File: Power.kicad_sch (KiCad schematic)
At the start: 21 parts

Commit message: Reset switch added
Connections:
- net 5V: no longer CP7.1, CP8.1, CP9.1, LP3.2, RP5.1, UP1.2 (VBIAS)
- new net MOT_POW: CP7.1, CP8.1, CP9.1, LP3.2, RP5.1, UP1.2 (VBIAS)
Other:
- note removed: "We need Motor power to be above 5 V say 5.2 or 5.5"
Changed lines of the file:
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@@
     (effects (font (size 1.778 1.778)) (justify left bottom))
   )
-  (text "We need Motor power to\nbe above 5 V say 5.2 or 5.5 \n"
-    (at 64.77 177.8 0)
-    (effects (font (size 1.27 1.27)) (justify left bottom))
-  )
-  (label "5V" (at 150.495 128.27 180)
+  (label "5V3" (at 150.495 128.27 180)
     (effects (font (size 1.27 1.27)) (justify right bottom))
   )

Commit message: MCU interfaces pulled out to parent sheet
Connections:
- net MCU_POW renamed 3V3
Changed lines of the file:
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@@
   (junction (at 138.43 139.7) (diameter 0) (color 0 0 0 0)
+  )
+  (junction (at 179.07 96.52) (diameter 0) (color 0 0 0 0)
   )
   (no_connect (at 107.95 132.08))
@@
     (stroke (width 0) (type default) (color 0 0 0 0))
   )
+  (wire (pts (xy 179.07 101.6) (xy 179.07 96.52))
+    (stroke (width 0) (type default) (color 0 0 0 0))
+  )
   (wire (pts (xy 114.935 35.56) (xy 120.65 35.56))
     (stroke (width 0) (type default) (color 0 0 0 0))
@@
   )
   (wire (pts (xy 138.43 164.465) (xy 138.43 168.275))
+    (stroke (width 0) (type default) (color 0 0 0 0))
+  )
+  (wire (pts (xy 196.85 101.6) (xy 179.07 101.6))
     (stroke (width 0) (type default) (color 0 0 0 0))
   )
@@
     (effects (font (size 1.27 1.27)) (justify left))
   )
+  (hierarchical_label "3V3" (shape bidirectional) (at 196.85 101.6 0)
+    (effects (font (size 1.27 1.27)) (justify left))
+  )

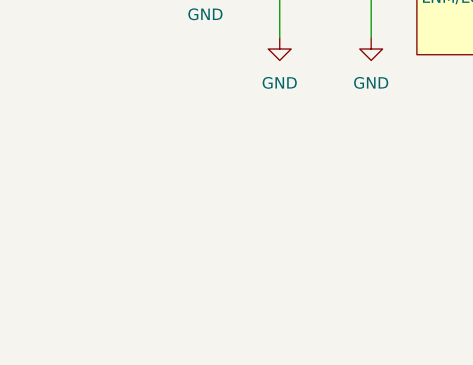
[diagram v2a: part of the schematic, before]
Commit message: MCU interfaces are done! Check the Changes and Complete ERC modifications
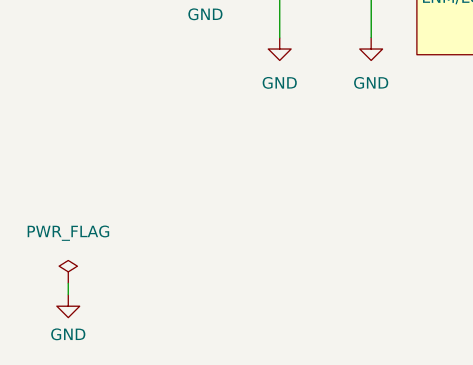
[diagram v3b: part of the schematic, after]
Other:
- company: (none) -> Parikshit Student Satellite Team
- title: (none) -> AOCS BOARD
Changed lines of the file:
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@@
 (kicad_sch (version 20211123) (generator eeschema)
   (paper "A4")
+  (title_block
+    (title "AOCS BOARD")
+    (company "Parikshit Student Satellite Team")
+  )
   (junction (at 63.5 33.02) (diameter 0) (color 0 0 0 0)
   )
@@
   )
   (wire (pts (xy 179.07 96.52) (xy 196.85 96.52))
+    (stroke (width 0) (type default) (color 0 0 0 0))
+  )
+  (wire (pts (xy 32.385 177.8) (xy 32.385 176.53))
     (stroke (width 0) (type default) (color 0 0 0 0))
   )
@@
     (pin "1")
   )
+  (symbol (lib_id "power:GND") (at 32.385 177.8 0) (unit 1)
+    (in_bom yes) (on_board yes) (fields_autoplaced)
+    (property "Reference" "#PWR0273" (id 0) (at 32.385 184.15 0)
+      (effects (font (size 1.27 1.27)) hide)
+    )
+    (property "Value" "GND" (id 1) (at 32.385 182.245 0))
+    (property "Footprint" "" (id 2) (at 32.385 177.8 0)
+      (effects (font (size 1.27 1.27)) hide)
+    )
+    (property "Datasheet" "" (id 3) (at 32.385 177.8 0)
+      (effects (font (size 1.27 1.27)) hide)
+    )
+    (pin "1")
+  )
   (symbol (lib_id "Device:C") (at 60.96 140.97 90) (unit 1)
     (in_bom yes) (on_board yes) (fields_autoplaced)
@@
     (pin "2")
   )
+  (symbol (lib_id "power:PWR_FLAG") (at 32.385 176.53 0) (unit 1)
+    (in_bom yes) (on_board yes) (fields_autoplaced)
+    (property "Reference" "#FLG0109" (id 0) (at 32.385 174.625 0)
+      (effects (font (size 1.27 1.27)) hide)
+    )
+    (property "Value" "PWR_FLAG" (id 1) (at 32.385 170.815 0))
+    (property "Footprint" "" (id 2) (at 32.385 176.53 0)
+      (effects (font (size 1.27 1.27)) hide)
+    )
+    (property "Datasheet" "~" (id 3) (at 32.385 176.53 0)
+      (effects (font (size 1.27 1.27)) hide)
+    )
+    (pin "1")
+  )
   (symbol (lib_id "power:GND") (at 170.18 45.085 0) (unit 1)

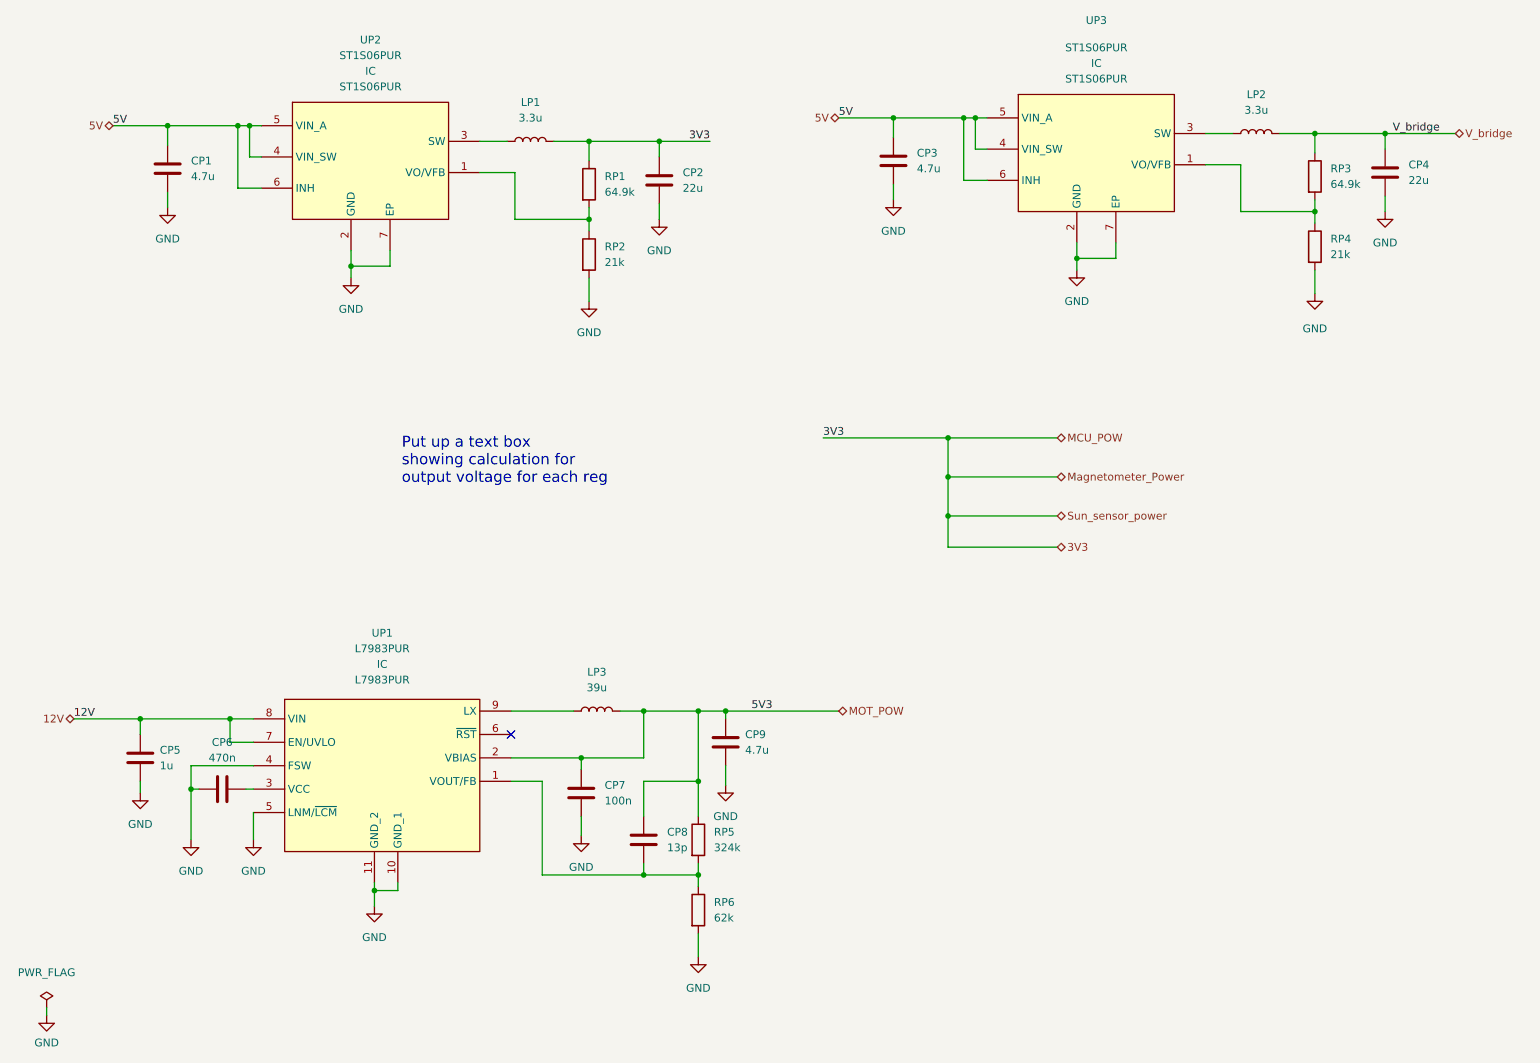
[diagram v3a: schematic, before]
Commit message: Max ERC errors corrected
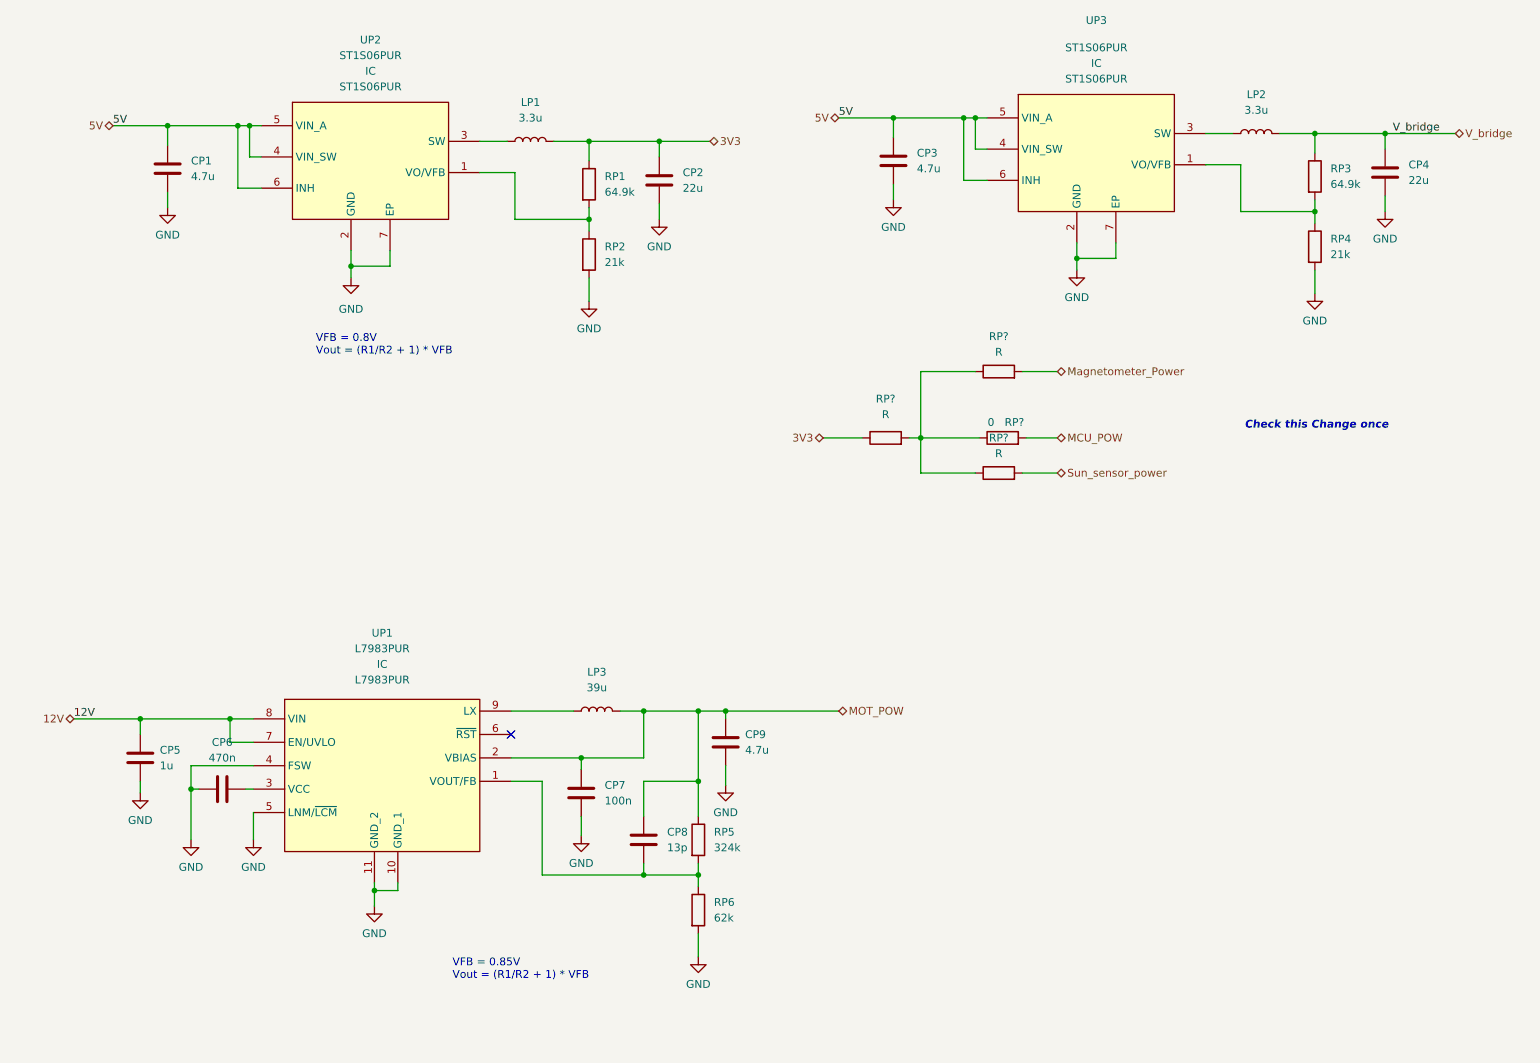
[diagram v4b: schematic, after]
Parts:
- added RP? (x3): R, symbol Device:R
- added RP?: 0, symbol Device:R
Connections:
- net 3V3: now also RP?.1
- new net: RP?.1, RP?.1, RP?.1, RP?.2
- new net MCU_POW: RP?.2
- new net Magnetometer_Power: RP?.2
- new net Sun_sensor_power: RP?.2
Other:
- note added: "Check this Change once"
- note added: "VFB = 0.85V Vout = (R1/R2 + 1) * VFB"
- note added: "VFB = 0.8V Vout = (R1/R2 + 1) * VFB"
- note removed: "Put up a text box showing calculation for output voltage for each reg"

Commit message: Updated the changes
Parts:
- gave numbers to parts that had none: 4
- renumbered CP3 to CP1, CP1 to CP2, CP4 to CP3, CP2 to CP4, CP9 to CP5, CP5 to CP6, CP6 to CP7, CP7 to CP8, CP8 to CP9, LP2 to LP1, LP1 to LP2, RP3 to RP1, RP6 to RP10, RP1 to RP2, RP4 to RP3, RP2 to RP4, RP5 to RP9, UP3 to UP1, UP1 to UP3

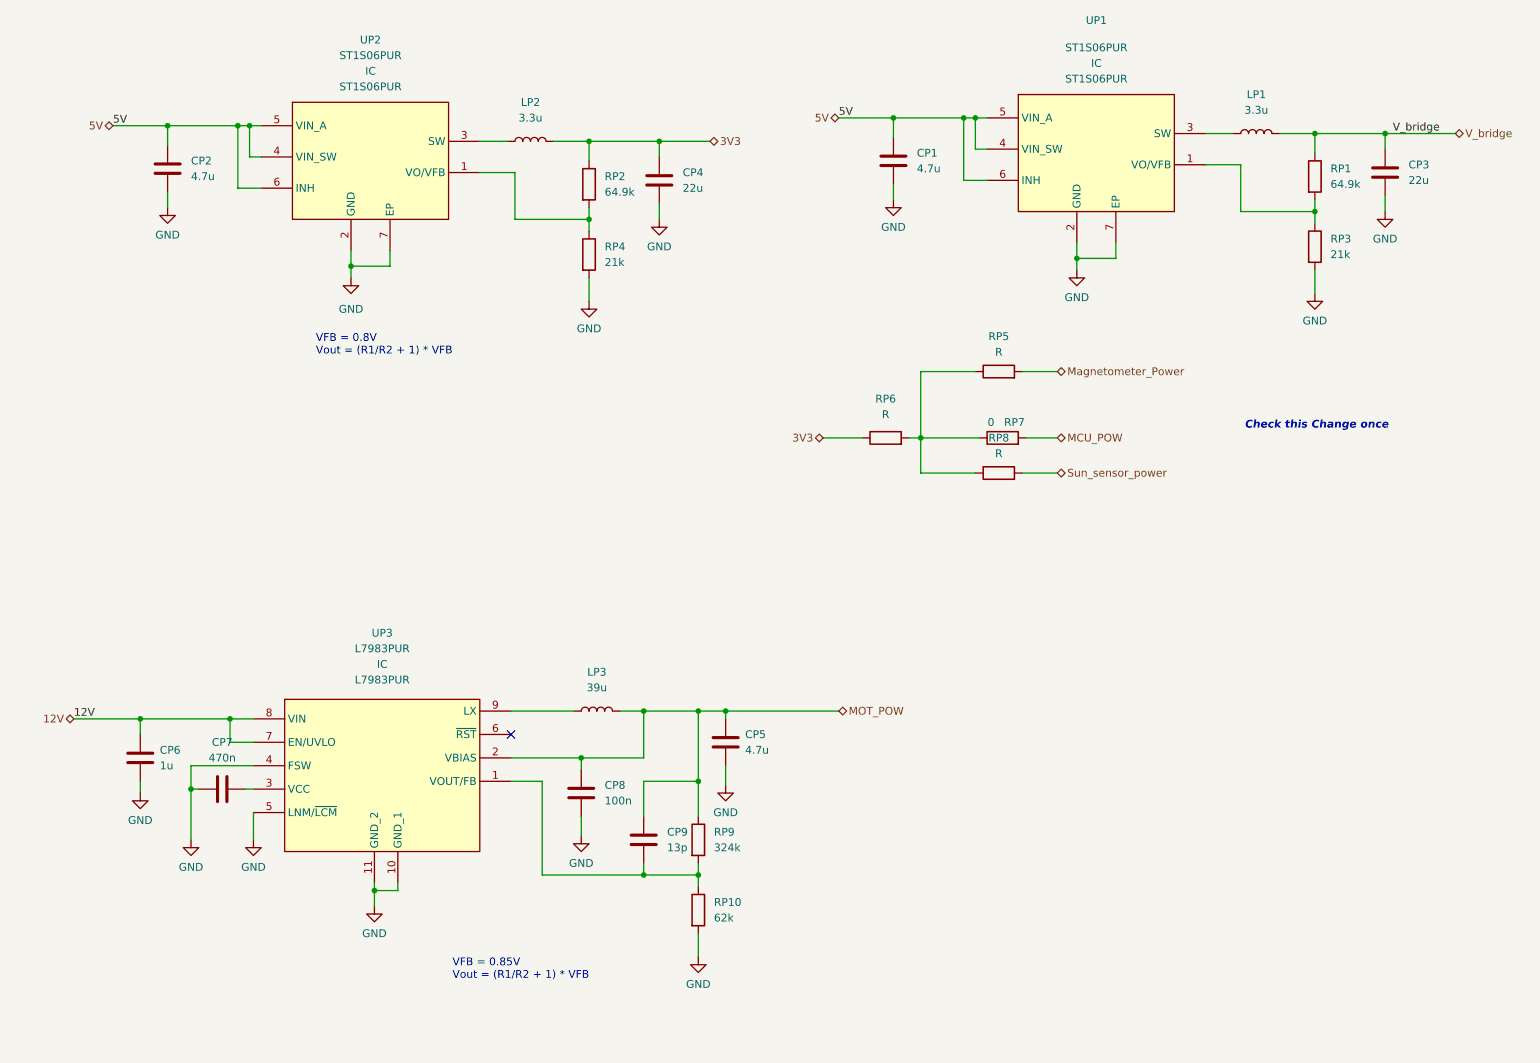
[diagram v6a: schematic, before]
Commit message: Placed NCs at ADCS_HMC1051
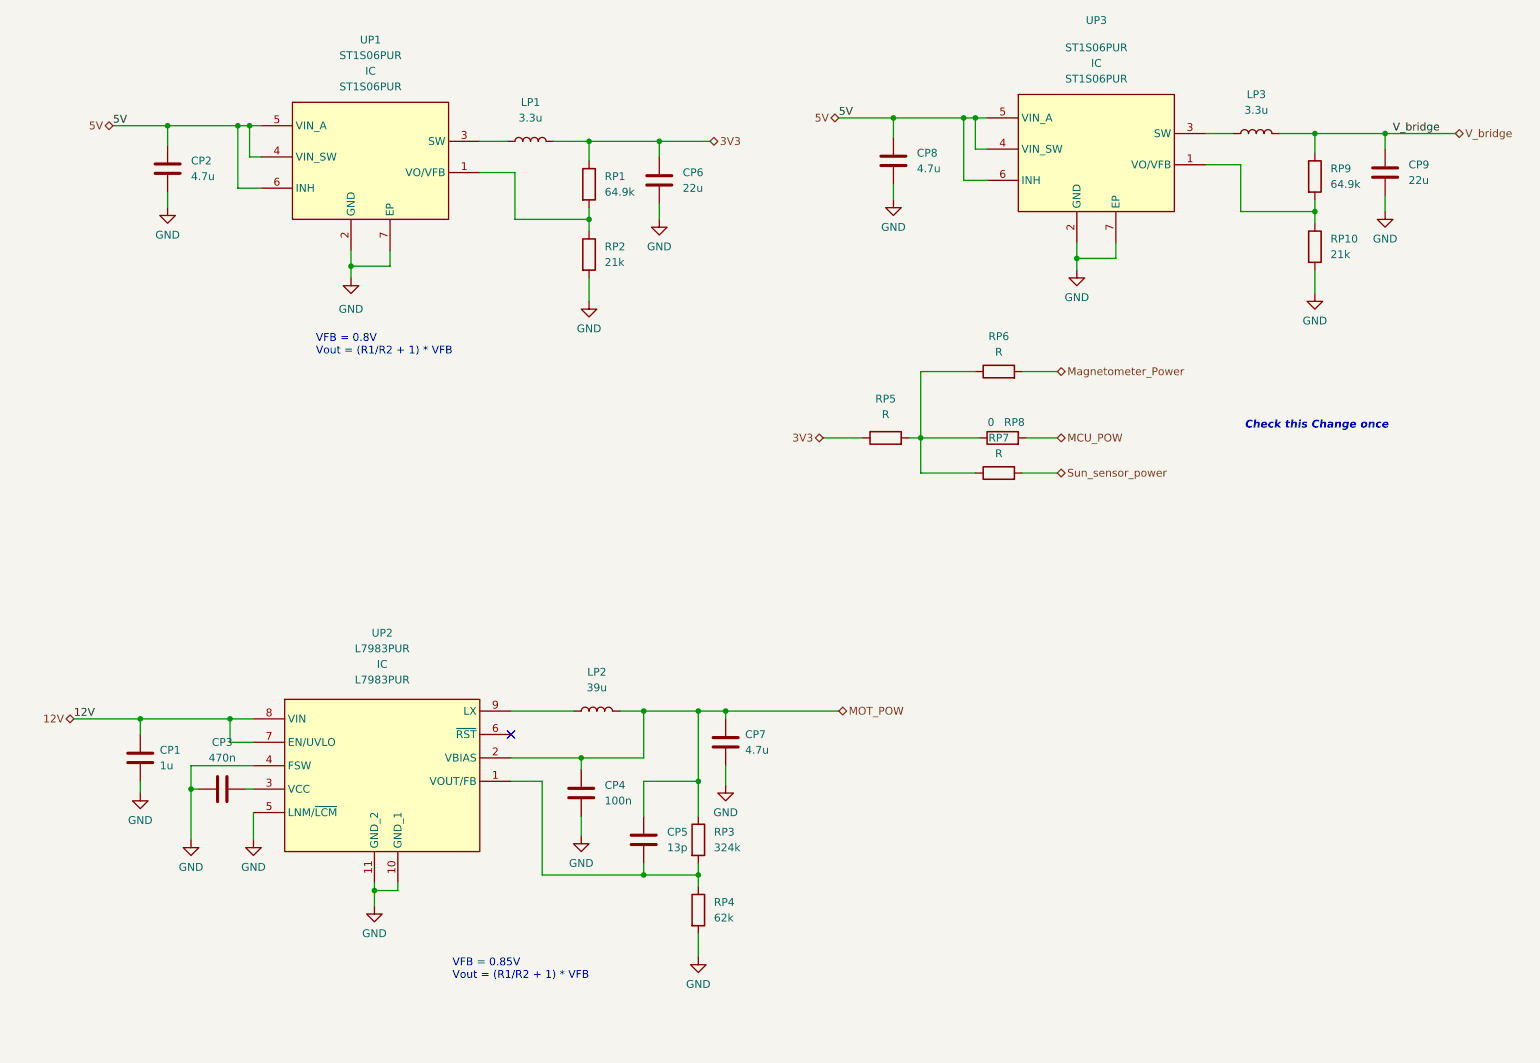
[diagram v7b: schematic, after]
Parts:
- renumbered CP6 to CP1, CP7 to CP3, CP8 to CP4, CP9 to CP5, CP4 to CP6, CP5 to CP7, CP1 to CP8, CP3 to CP9, LP2 to LP1, LP3 to LP2, LP1 to LP3, RP2 to RP1, RP3 to RP10, RP4 to RP2, RP9 to RP3, RP10 to RP4, RP6 to RP5, RP5 to RP6, RP8 to RP7, RP7 to RP8, RP1 to RP9, UP2 to UP1, UP3 to UP2, UP1 to UP3
